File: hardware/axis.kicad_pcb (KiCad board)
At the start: 4 copper layers, 66 x 17.5 mm, 43 parts, among them J101 Cortex, J102 DX07S016JA3, SW101 SKSG, SW102 SKSG, U101 TPS78433QWDRBRQ1, U102 ATSAMD51G, U103 BMM150, U104 BHI160, Y101 32k768

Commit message: Export stencil
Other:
- board text removed: "2026-02-07 stencil"

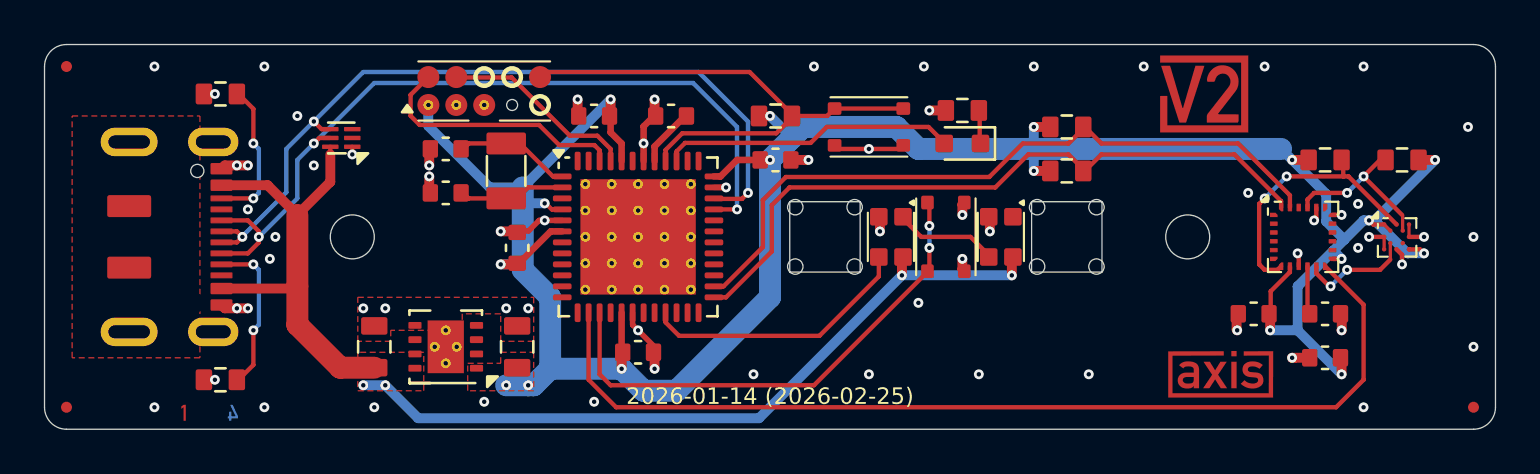
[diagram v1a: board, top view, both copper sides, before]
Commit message: Update ESD suppressor
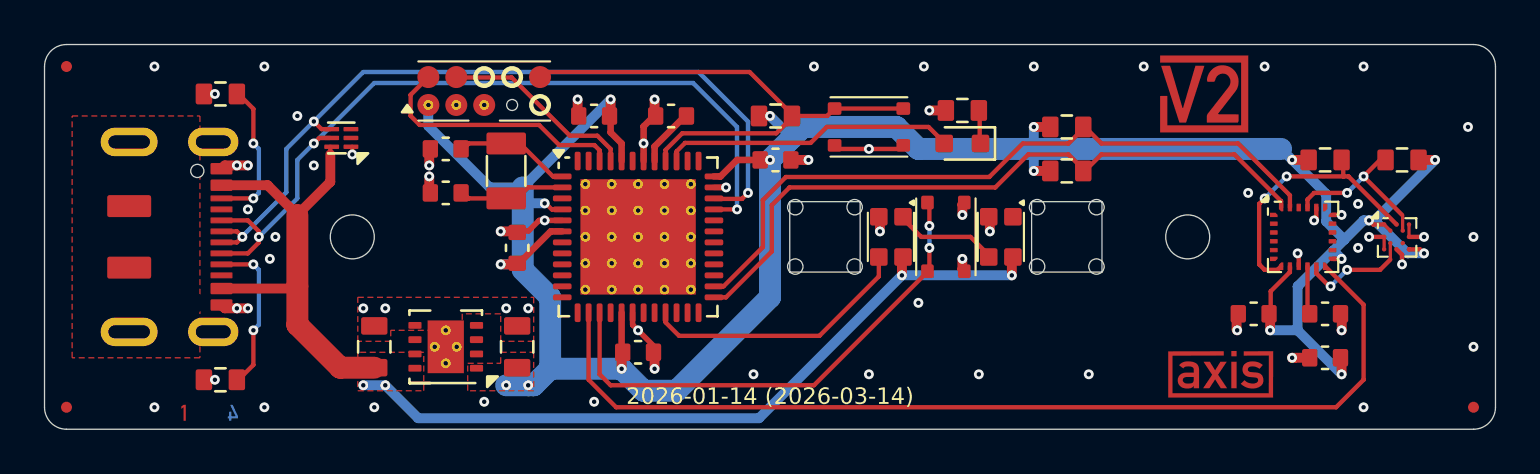
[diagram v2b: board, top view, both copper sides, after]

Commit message: KiCad 10
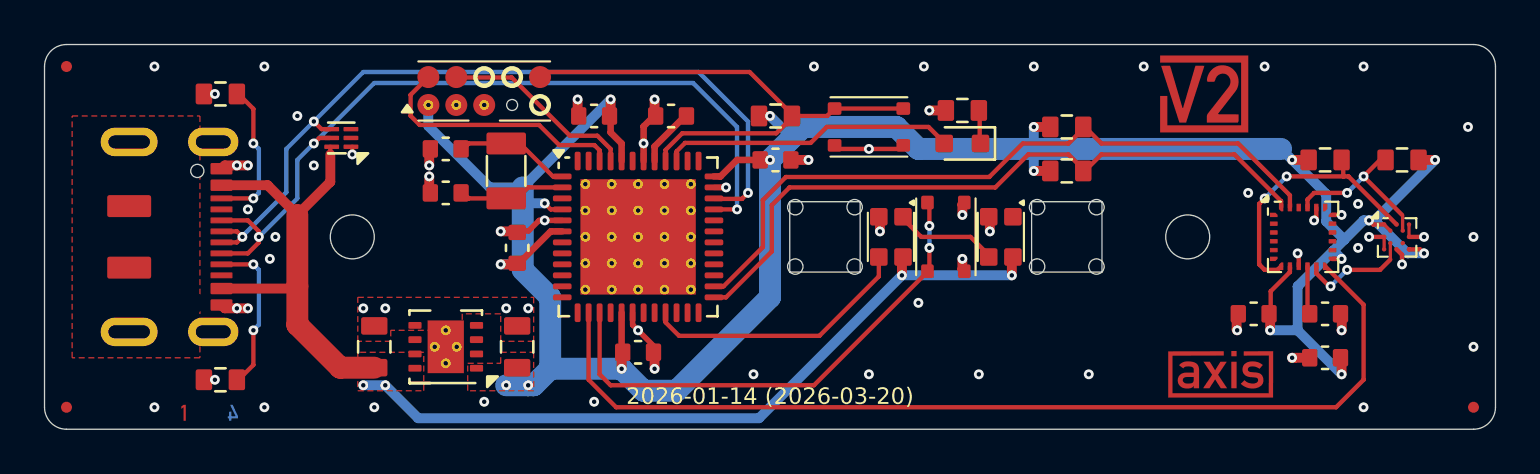
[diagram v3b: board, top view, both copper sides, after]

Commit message: Update
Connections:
- net /VDDCORE renamed /+VDDCORE
- net Shield renamed /Shield

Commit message: Update
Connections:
- net /+VDDCORE renamed /+VCORE

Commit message: Update DRC
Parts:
- renumbered C108 to C101, C109 to C102, C101 to C103, C110 to C104, C112 to C105, C102 to C106, C103 to C107, C104 to C108, C105 to C109, C111 to C110, C106 to C111, C107 to C112, D103 to D101, D101 to D102, D102 to D103, INFO102 to INFO101, INFO101 to INFO102, R105 to R101, R106 to R102, R104 to R103, R107 to R104, R108 to R105, R101 to R106, R102 to R107, R103 to R108, SW102 to SW101, SW101 to SW102, U104 to U101, U101 to U104
